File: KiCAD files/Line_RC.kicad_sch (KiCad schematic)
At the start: 15 parts, among them IC1 ESP32-WROVER-E-N4R8, IC2 CP2102N-A02-GQFN28R, IC3 TLV75533PDBVR

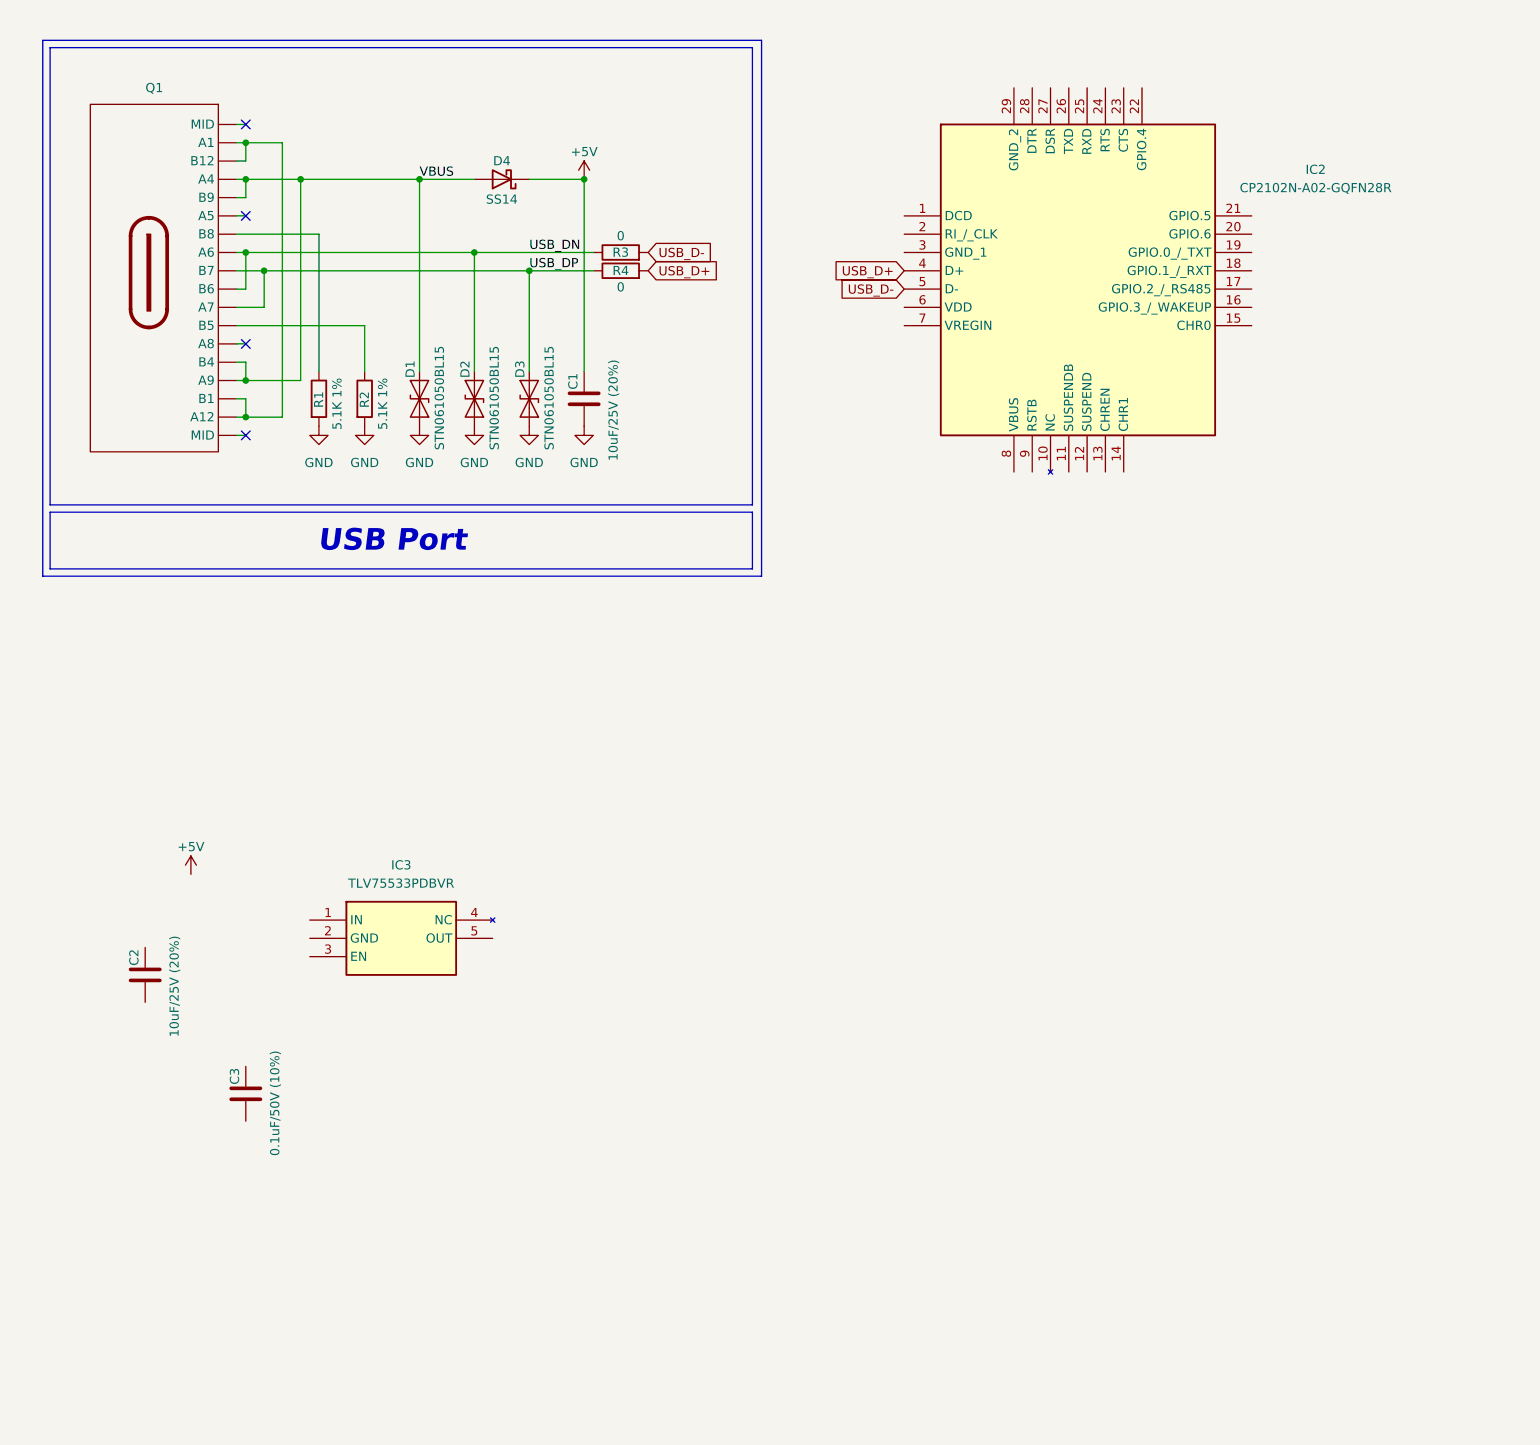
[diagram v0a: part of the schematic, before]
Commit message: Added schematic block for USB to UART conversion
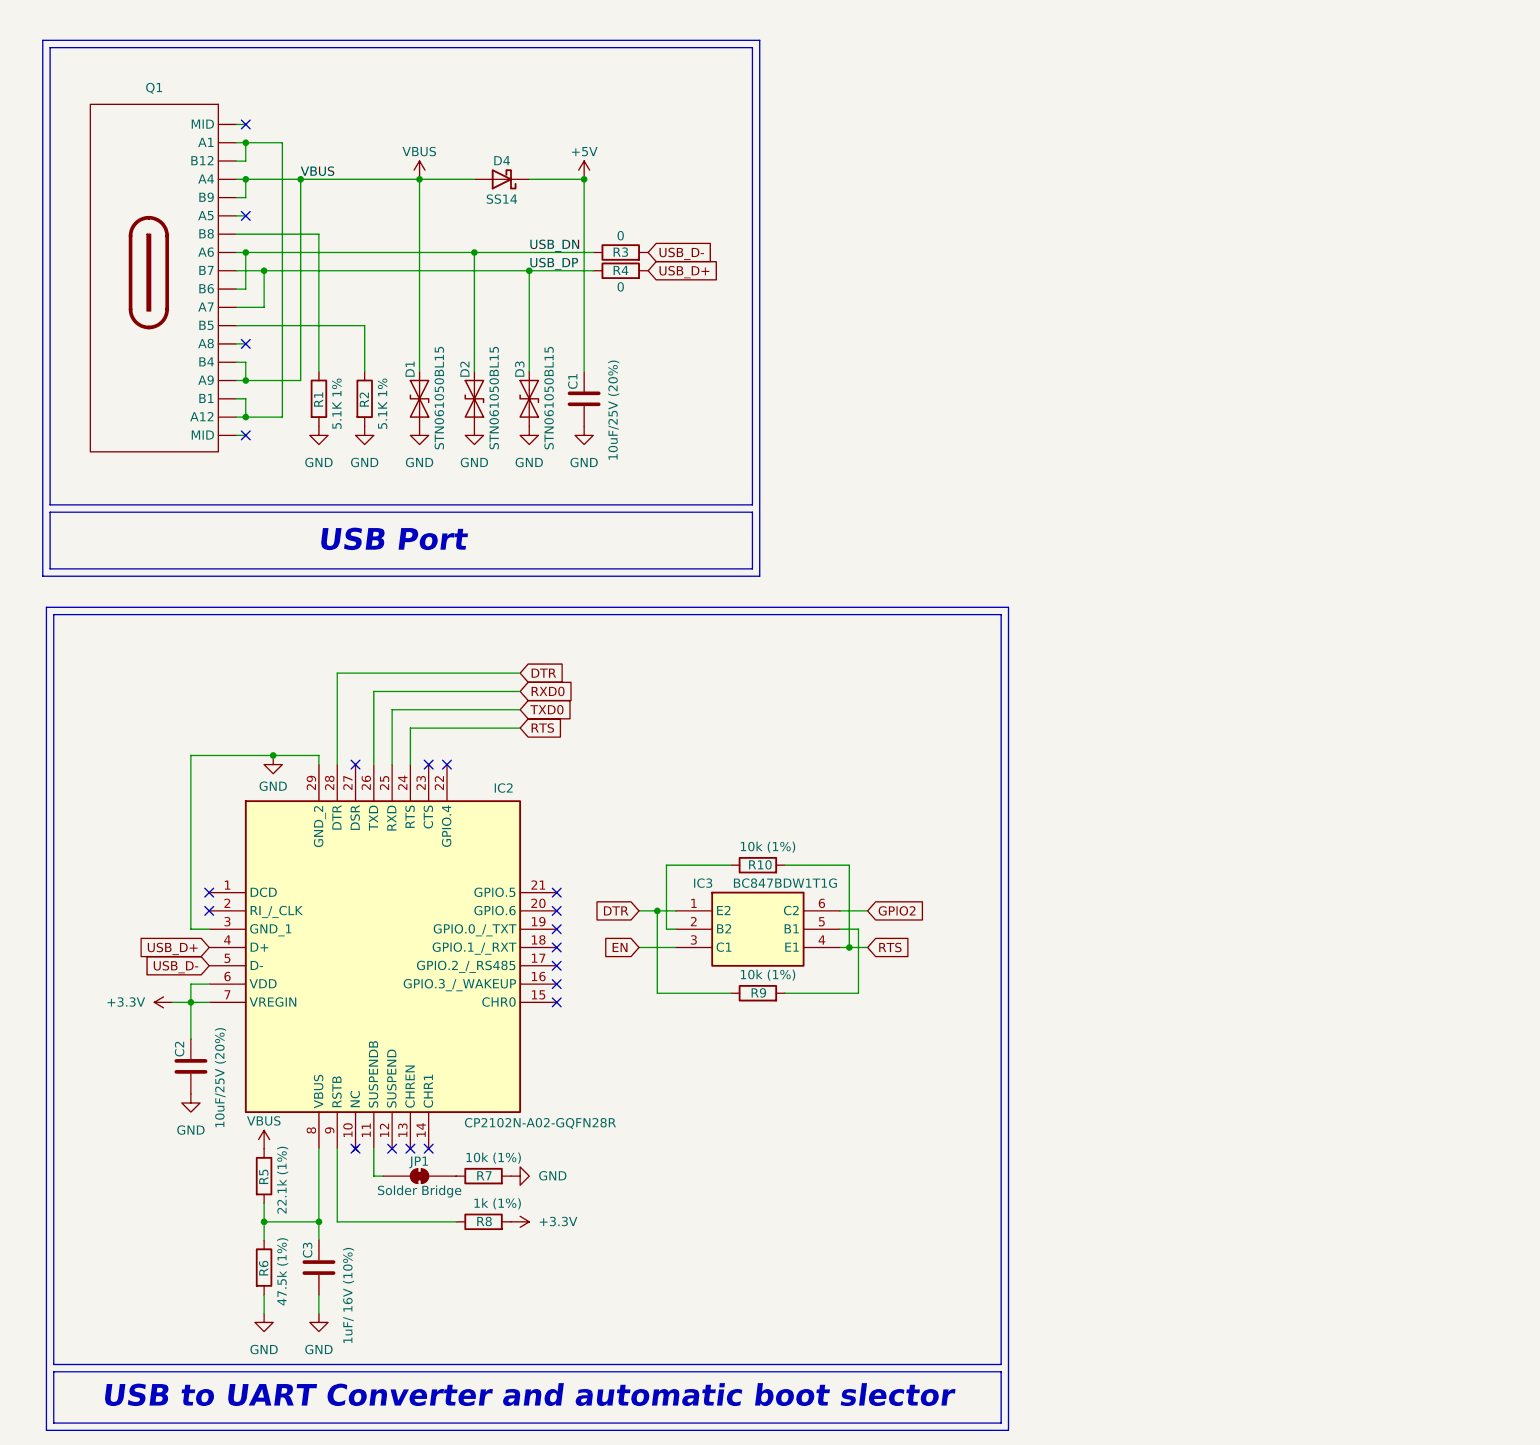
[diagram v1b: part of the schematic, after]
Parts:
- removed IC3: TLV75533PDBVR, SOT95P280X145-5N, symbol TLV75533PDBVR:TLV75533PDBVR
- added IC3: BC847BDW1T1G, SOT65P210X110-6N, symbol BC847BDW1T1G:BC847BDW1T1G
- added JP1: Solder Bridge, symbol Jumper:SolderJumper_2_Bridged
- added R10, R7, R9: 10k (1%), symbol Device:R
- added R5: 22.1k (1%), symbol Device:R
- added R6: 47.5k (1%), symbol Device:R
- added R8: 1k (1%), symbol Device:R
- C3: value 0.1uF/50V (10%) -> 1uF/ 16V (10%)
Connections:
- net GND: now also C2.2, C3.2, IC2.29 (GND_2), IC2.3 (GND_1), R6.2, R7.2
- net VBUS: now also R5.1
- net at C3.1: now also IC2.8 (VBUS), R5.2, R6.1
- net +3.3V: now reaches C2.1
- net +3.3V: now also IC2.6 (VDD), IC2.7 (VREGIN), R8.2
- net at IC2.11 (SUSPENDB): now also JP1.1 (A)
- net RTS: now reaches IC2.24 (RTS)
- net RTS: now also IC3.4 (E1), R10.2
- net TXD0: now reaches IC2.25 (RXD)
- net RXD0: now reaches IC2.26 (TXD)
- net DTR: now reaches IC2.28 (DTR)
- net DTR: now also IC3.1 (E2), R9.1
- net at IC2.9 (RSTB): now also R8.1
- new net: IC3.2 (B2), R10.1
- new net: IC3.5 (B1), R9.2
- new net: JP1.2 (B), R7.1
- new net EN: IC3.3 (C1)
- new net GPIO2: IC3.6 (C2)
- no-connect marks 4 -> 20
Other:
- note added: "USB to UART Converter and automatic boot slector"
- moved on the sheet: IC2

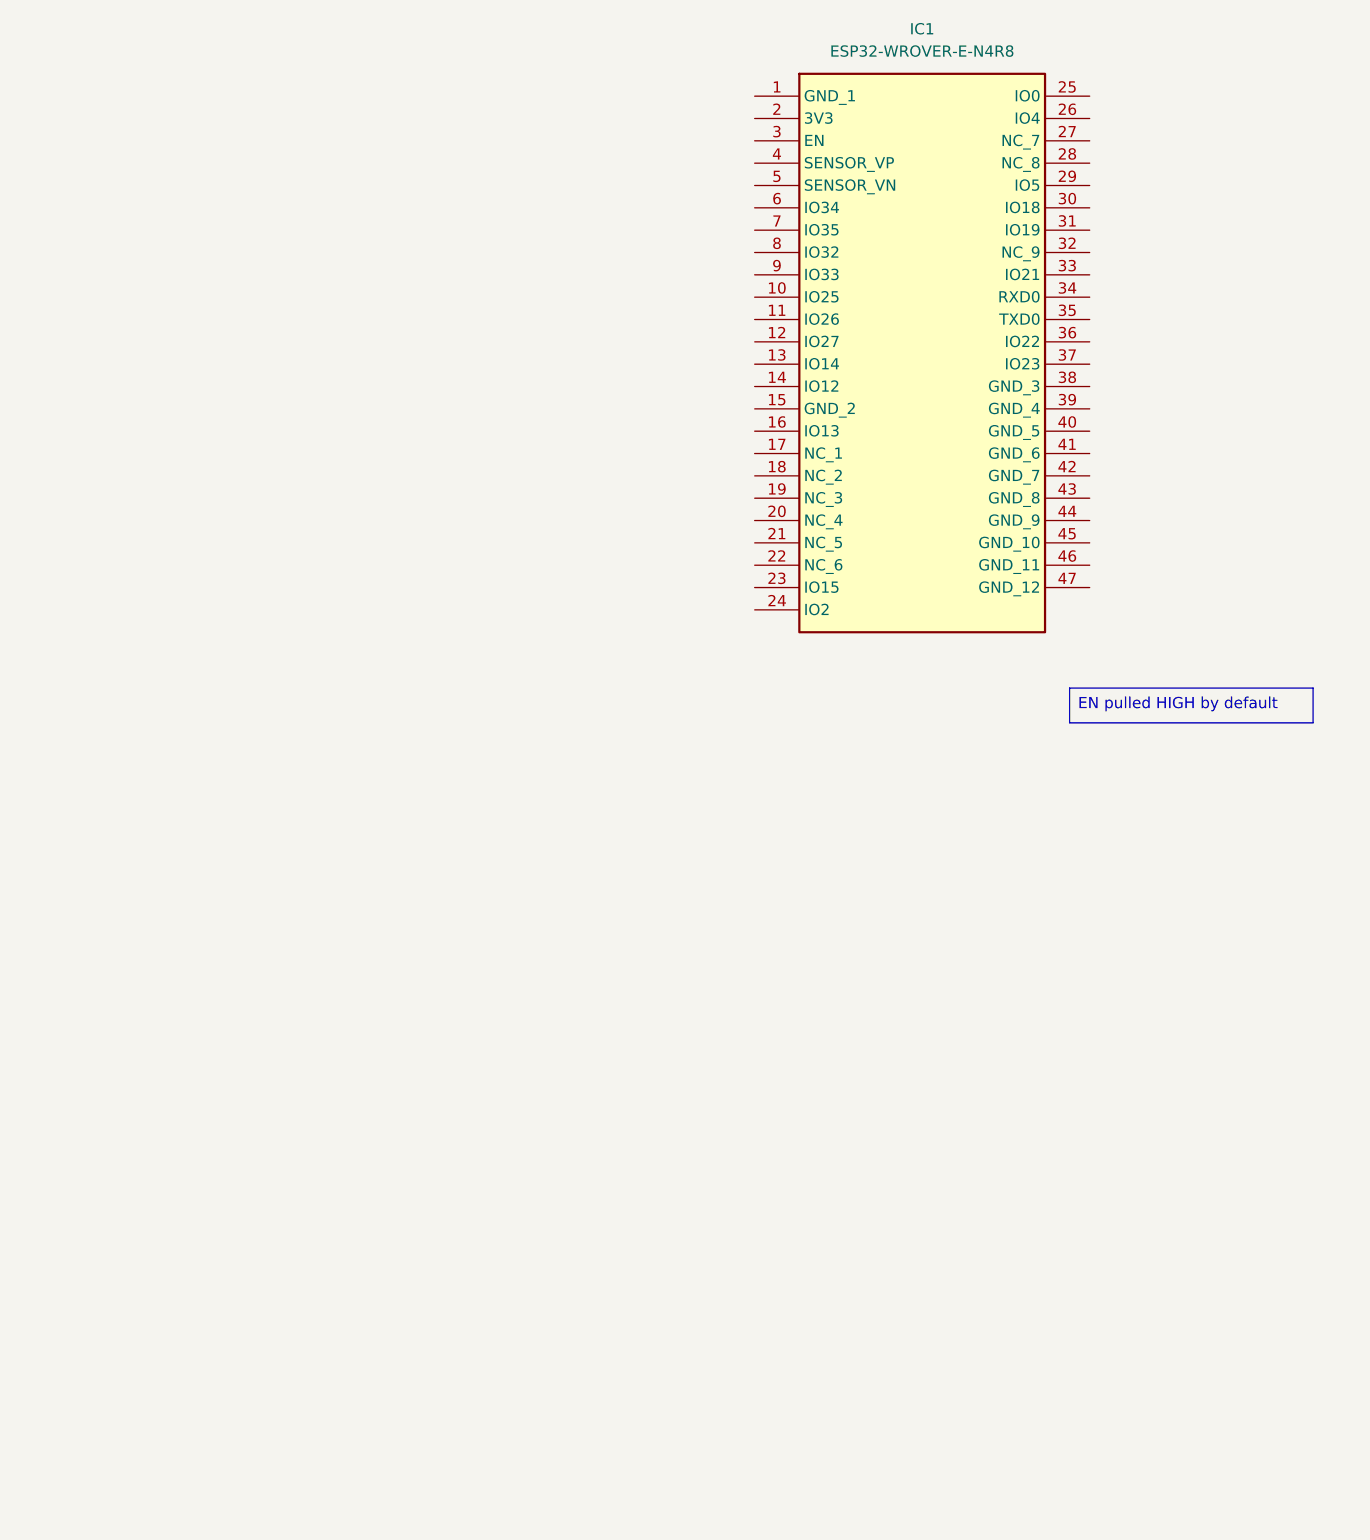
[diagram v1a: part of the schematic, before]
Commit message: Added filtering caps and EN pullup
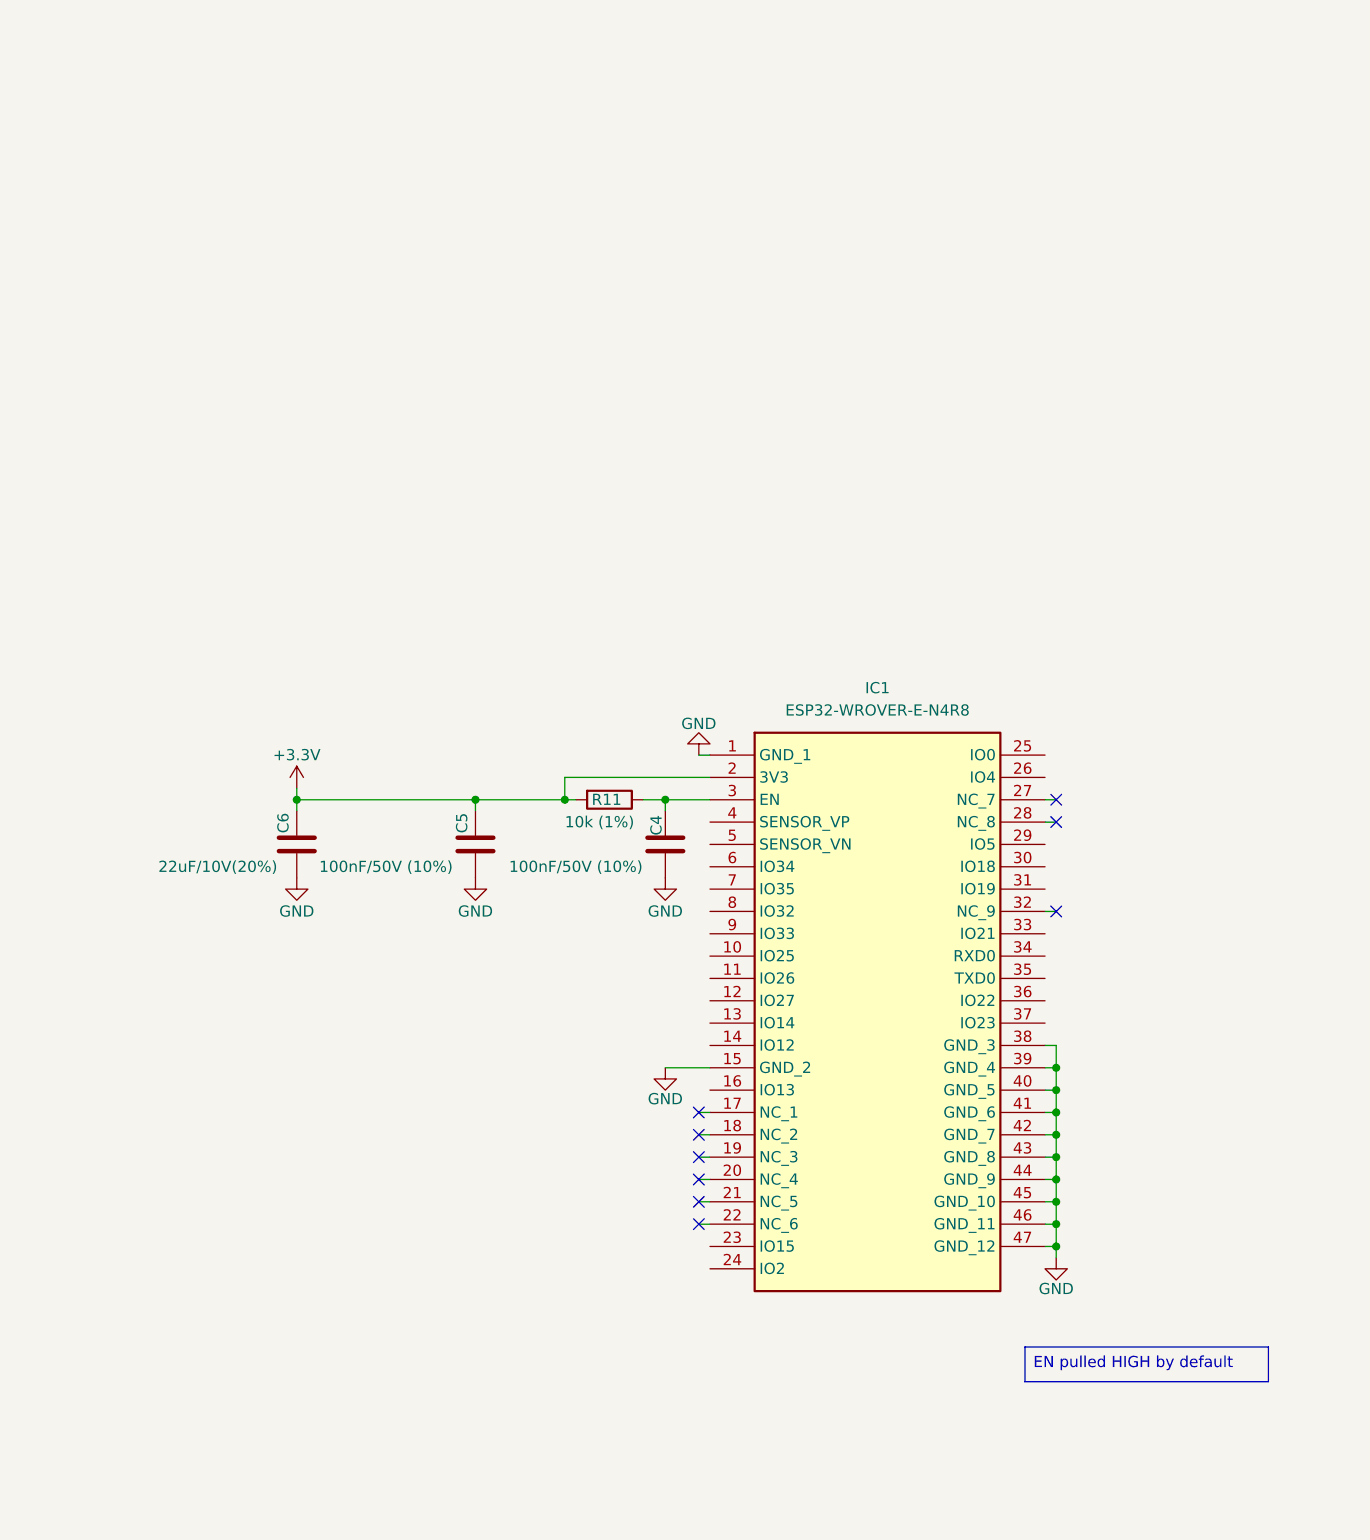
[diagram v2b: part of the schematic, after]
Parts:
- added C4, C5: 100nF/50V (10%), symbol Device:C
- added C6: 22uF/10V(20%), symbol Device:C
- added R11: 10k (1%), symbol Device:R
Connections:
- net +3.3V: now also IC1.2 (3V3), C5.1, C6.1, R11.2
- net GND: now also IC1.1 (GND_1), IC1.15 (GND_2), IC1.38 (GND_3), IC1.39 (GND_4), IC1.40 (GND_5), IC1.41 (GND_6), IC1.42 (GND_7), IC1.43 (GND_8), IC1.44 (GND_9), IC1.45 (GND_10), IC1.46 (GND_11), IC1.47 (GND_12), C4.2, C5.2, C6.2
- net at IC1.3 (EN): now also C4.1, R11.1
- no-connect marks 20 -> 29
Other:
- moved on the sheet: IC1
